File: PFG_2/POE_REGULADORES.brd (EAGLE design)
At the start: 119.6 x 95.9 mm, 185 parts, among them J1 1-406541-1, J10 OSTVN04A150, J2 AMPS_Connect, J3 Port Current, J4 OSTVN04A150, J5 TB001-500-02BE, J6 OSTVN02A150, J7 OSTVN02A150, J8 TB001-500-02BE, J9 TB001-500-02BE, Q1 FDN8601, Q2 FDN8601, Q3 FDN8601, Q4 FDN8601, Q5 CSD18533Q5A, Q6 CSD18533Q5A, T1 750313355, U1 7490220122, U10 12V, U11 FCX493TA, U12 TL431AIDBVR, U13 LM5165DRCR, U14 ENC28J60-I/SP, U2 TPS2373-3RGWT, U3 UCC2897APW, U4 12V, U5 FCX493TA, U6 TCMT1107, U7 MMBT3906, U8 FDMS86250, U9 IRFR9220PBF, Y1 Crystal_25Mhz

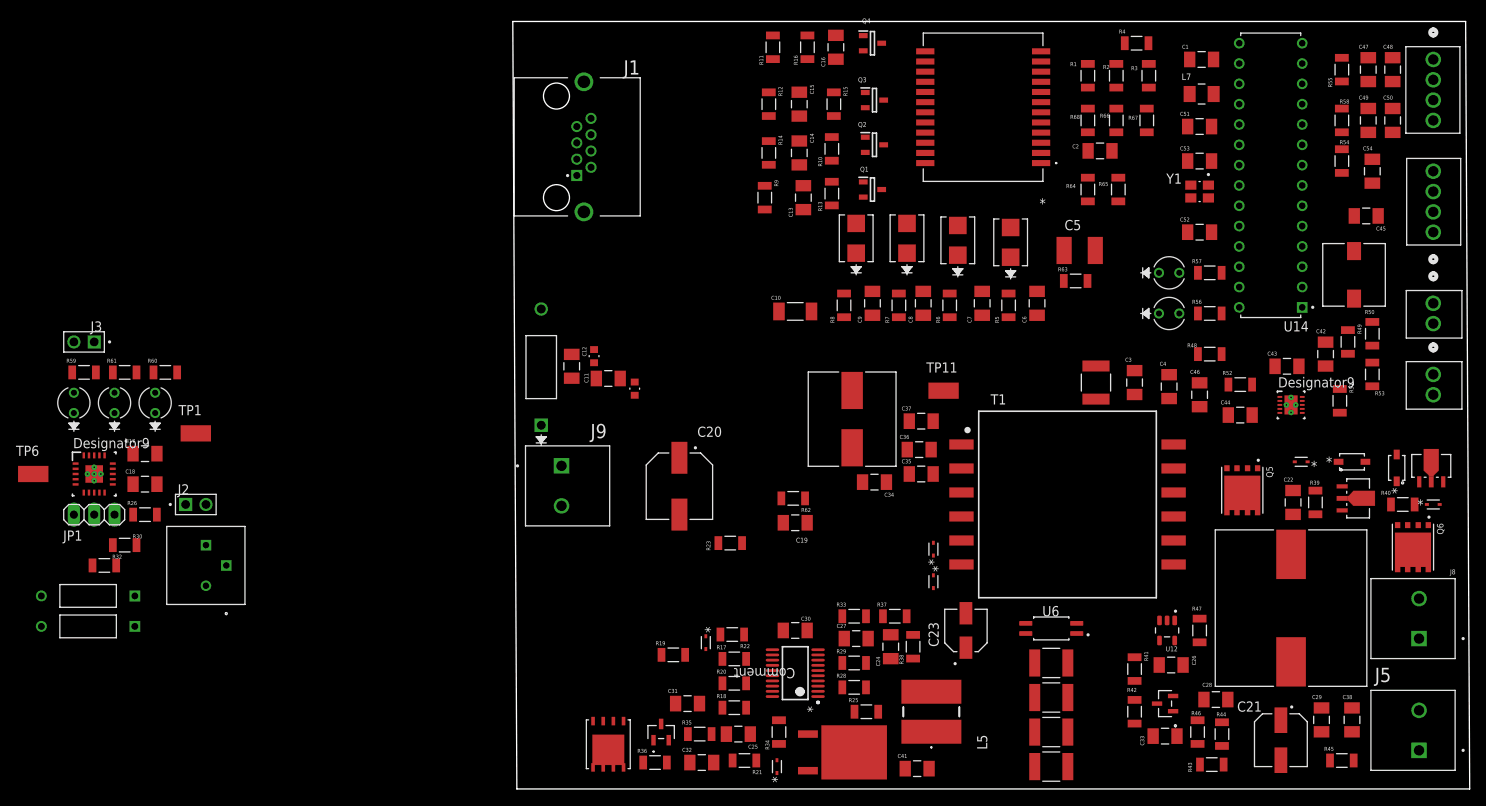
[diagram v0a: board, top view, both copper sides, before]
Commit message: Colocados componentes y planos RTN, GND, VDD, VSS, 3V3, 12V
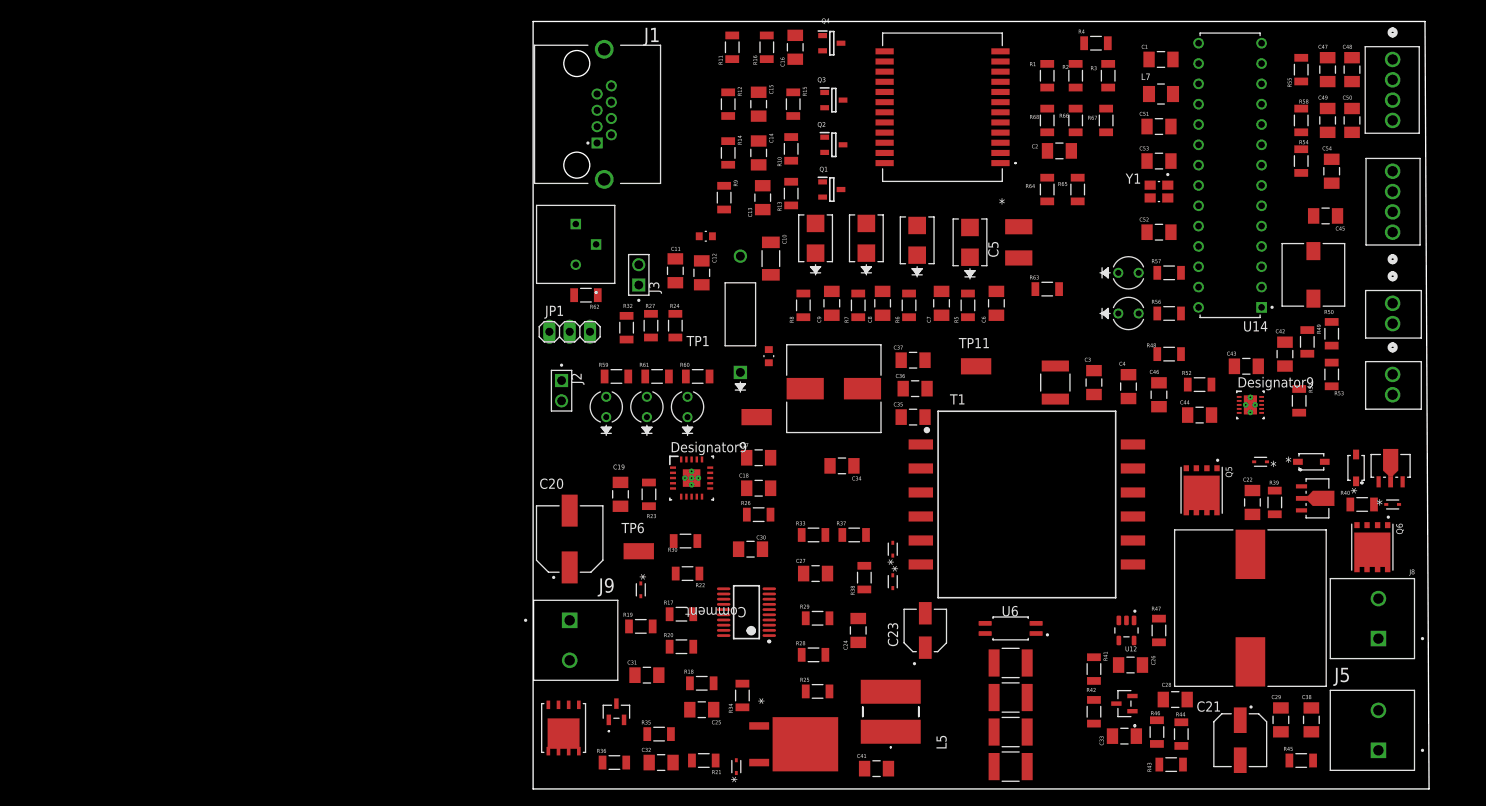
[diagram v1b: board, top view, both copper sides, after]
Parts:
- R24, R27: device R24:YAG_MF25_YAG -> RC1206FR-071ML:RESC3116X65N
- moved R24 77.3 mm to (19.8, 57.9), turned to 270 degrees
- moved C17 76.7 mm to (30.2, 41.4)
- moved C18 76.7 mm to (30.2, 37.6)
- moved R26 76.7 mm to (30.2, 34.3)
- moved TP6 76.3 mm to (15.2, 29.7)
- moved U2 74.7 mm to (21.8, 38.9)
- moved R27 72.8 mm to (16.8, 57.9), turned to 270 degrees
- moved R32 71.7 mm to (13.7, 57.7), turned to 270 degrees
- moved TP1 70.1 mm to (30.0, 46.5)
- moved R30 70.1 mm to (21.1, 31.0), turned to 0 degrees
- moved J3 69.8 mm to (15.2, 64.3), turned to 90 degrees
- moved LED1 66.5 mm to (16.3, 46.5)
- moved LED2 66.5 mm to (21.3, 46.5)
- moved LED3 66.5 mm to (11.2, 46.5)
- moved R59 66.5 mm to (12.4, 51.6)
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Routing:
- added copper zone on layer 15, net VSS
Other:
- board size 119.6 x 95.9 mm -> 112 x 95.9 mm

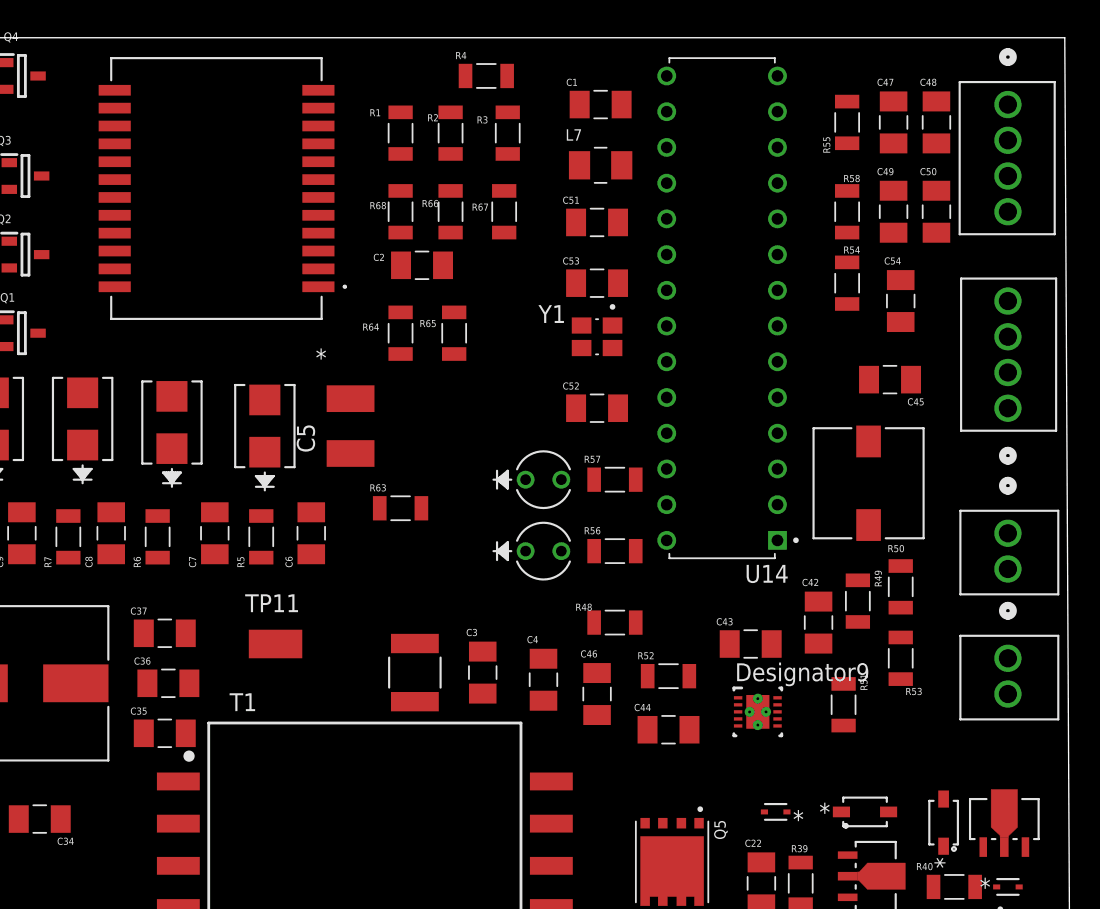
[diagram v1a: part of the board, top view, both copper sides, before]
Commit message: Colocadas pistas de zona 3V3
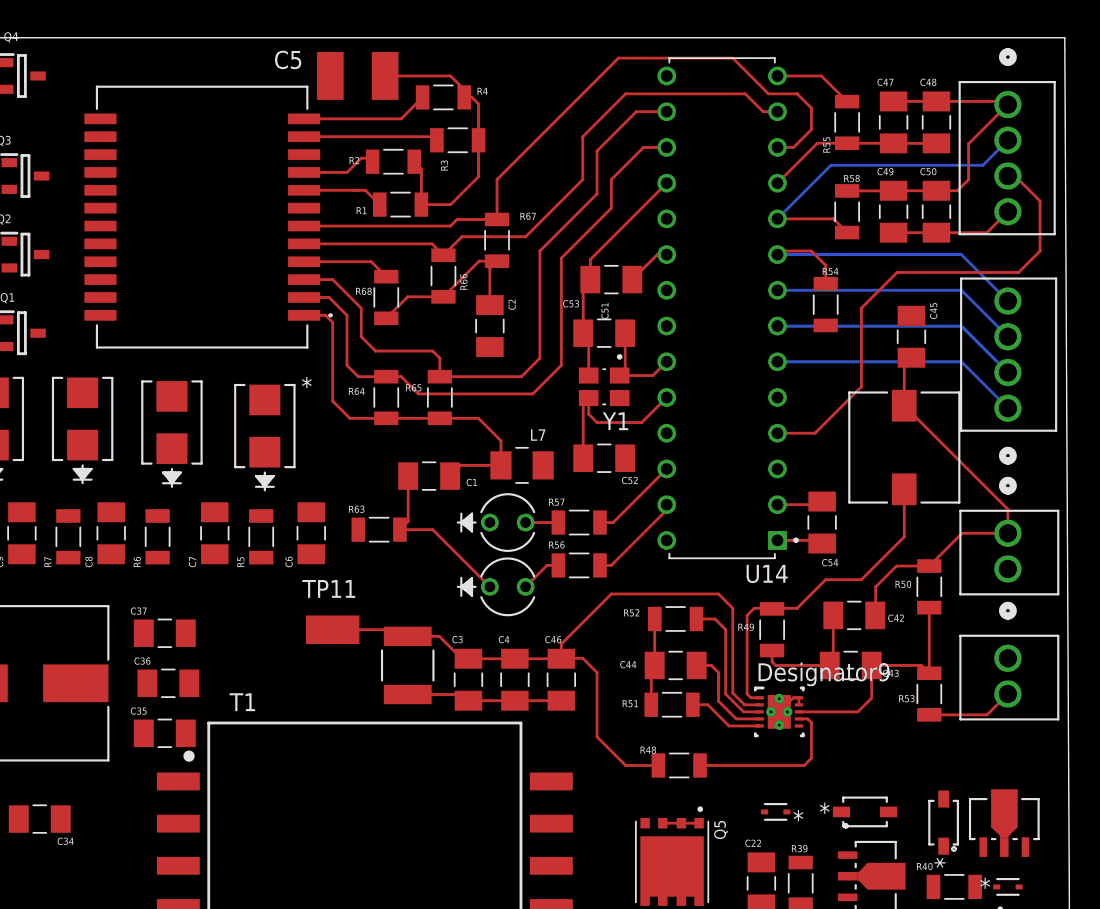
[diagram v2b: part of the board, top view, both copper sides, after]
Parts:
- moved C1 29.1 mm to (68.3, 64.8), turned to 180 degrees
- moved C5 24.9 mm to (63.2, 93.2), turned to 0 degrees
- moved L7 22.1 mm to (74.9, 65.5)
- moved C54 16.7 mm to (96.3, 61.5), turned to 270 degrees
- moved R51 12.2 mm to (85.6, 48.5), turned to 0 degrees
- moved R48 11.1 mm to (86.1, 44.2)
- moved C43 7.27 mm to (98.3, 51.3), turned to 180 degrees
- moved C2 6.48 mm to (72.6, 75.4), turned to 270 degrees
- moved R49 6.43 mm to (92.7, 53.8)
- moved R68 6.18 mm to (65.3, 77.5)
- moved R1 5.08 mm to (66.3, 84.1), turned to 0 degrees
- moved R65 4.68 mm to (69.1, 70.4)
- moved R64 4.68 mm to (65.3, 70.4)
- moved C44 4.60 mm to (85.9, 51.3)
- moved R66 4.60 mm to (69.3, 79.0)
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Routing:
- net GND: track 0.00 -> 81.3 mm
- net +3V3: track 0.00 -> 55.6 mm
- net VDD_P: track 0.00 -> 54.8 mm
- net RXD_N: track 0.00 -> 48.6 mm
- net TXD_N: track 0.00 -> 44.7 mm
- net TXD_P: track 0.00 -> 44.1 mm
- net RXD_P: track 0.00 -> 41.1 mm
- net N_INT: track 0.00 -> 33.9 mm
- net TXD_CT: track 0.00 -> 27.4 mm
- net RESET_ETH: track 0.00 -> 24.1 mm
- net N$70: track 0.00 -> 23.5 mm
- net CS: track 0.00 -> 23.0 mm
- net N$17: track 0.00 -> 21.1 mm
- net SPI_MOSI: track 0.00 -> 17.8 mm
- net SPI_SCLK: track 0.00 -> 17.8 mm
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
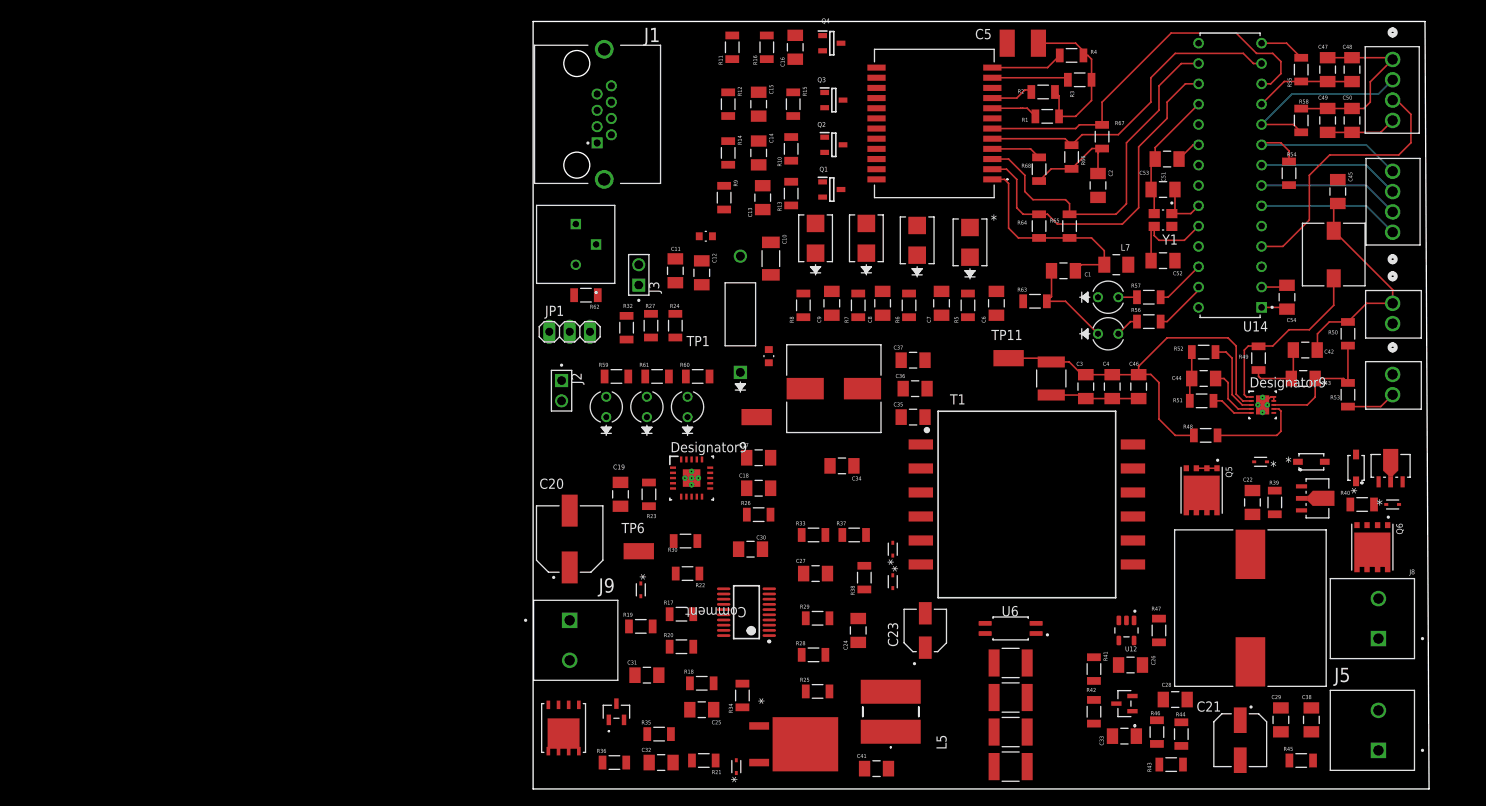
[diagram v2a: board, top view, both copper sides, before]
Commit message: Colocadas vias GND y RTN
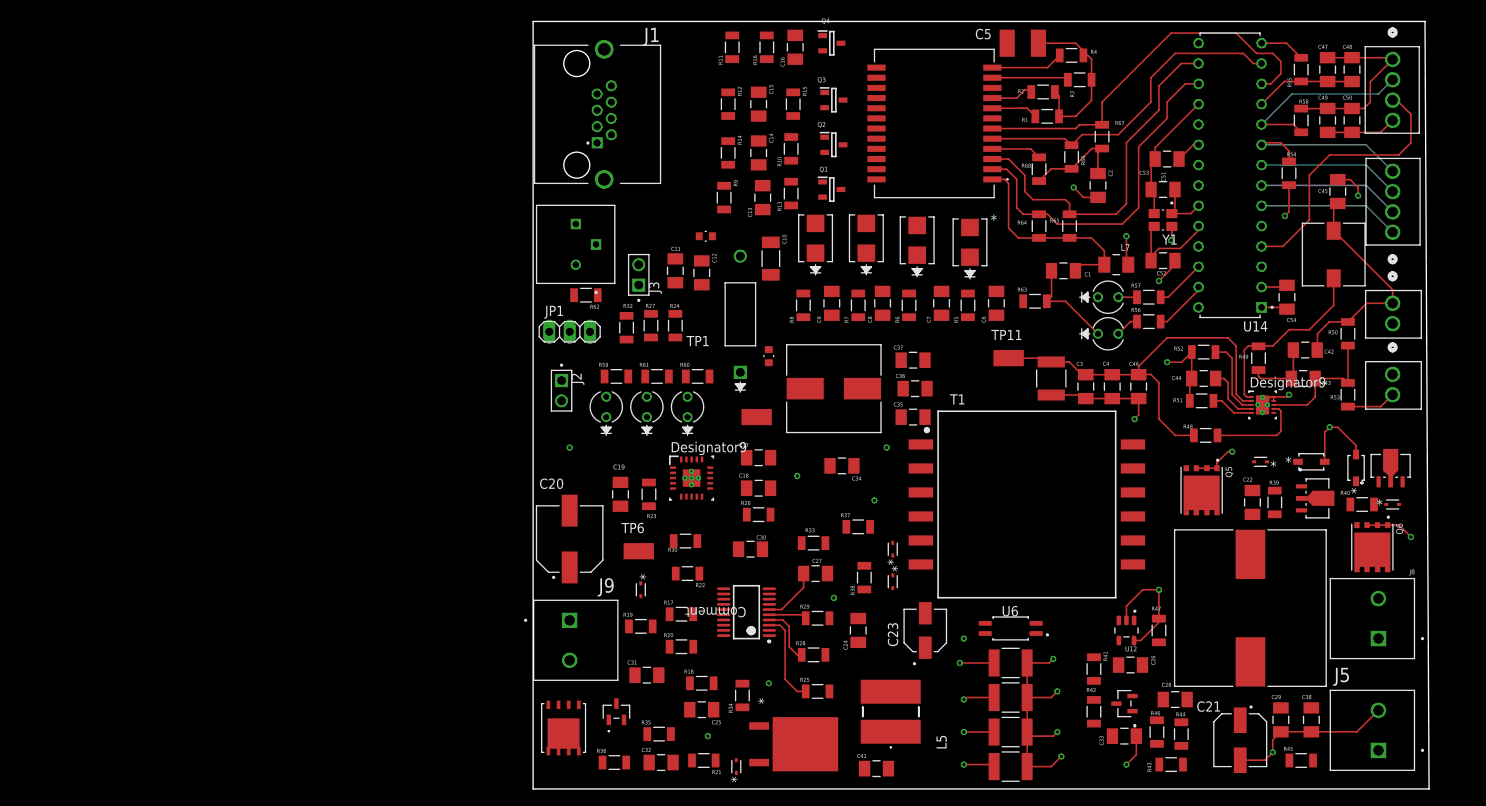
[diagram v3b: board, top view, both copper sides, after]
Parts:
- moved R37 1.14 mm to (42.7, 32.8)
- moved R33 1.02 mm to (37.1, 30.7), turned to 180 degrees
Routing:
- net GND: track 81.3 -> 190.6 mm, vias 0 -> 17
- net RTN: track 0.00 -> 15.8 mm, vias 0 -> 12
- net N$44: track 0.00 -> 11.6 mm
- net +3V3: track 55.6 -> 63.3 mm, vias 0 -> 2
- net N$45: track 0.00 -> 7.35 mm
- net N$48: track 0.00 -> 7.18 mm
- net N$46: track 0.00 -> 4.74 mm
- net OSC2: track 12.1 -> 12.8 mm

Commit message: Colocadas vias GND, RTN en cada componente, redistribución de componentes 12V
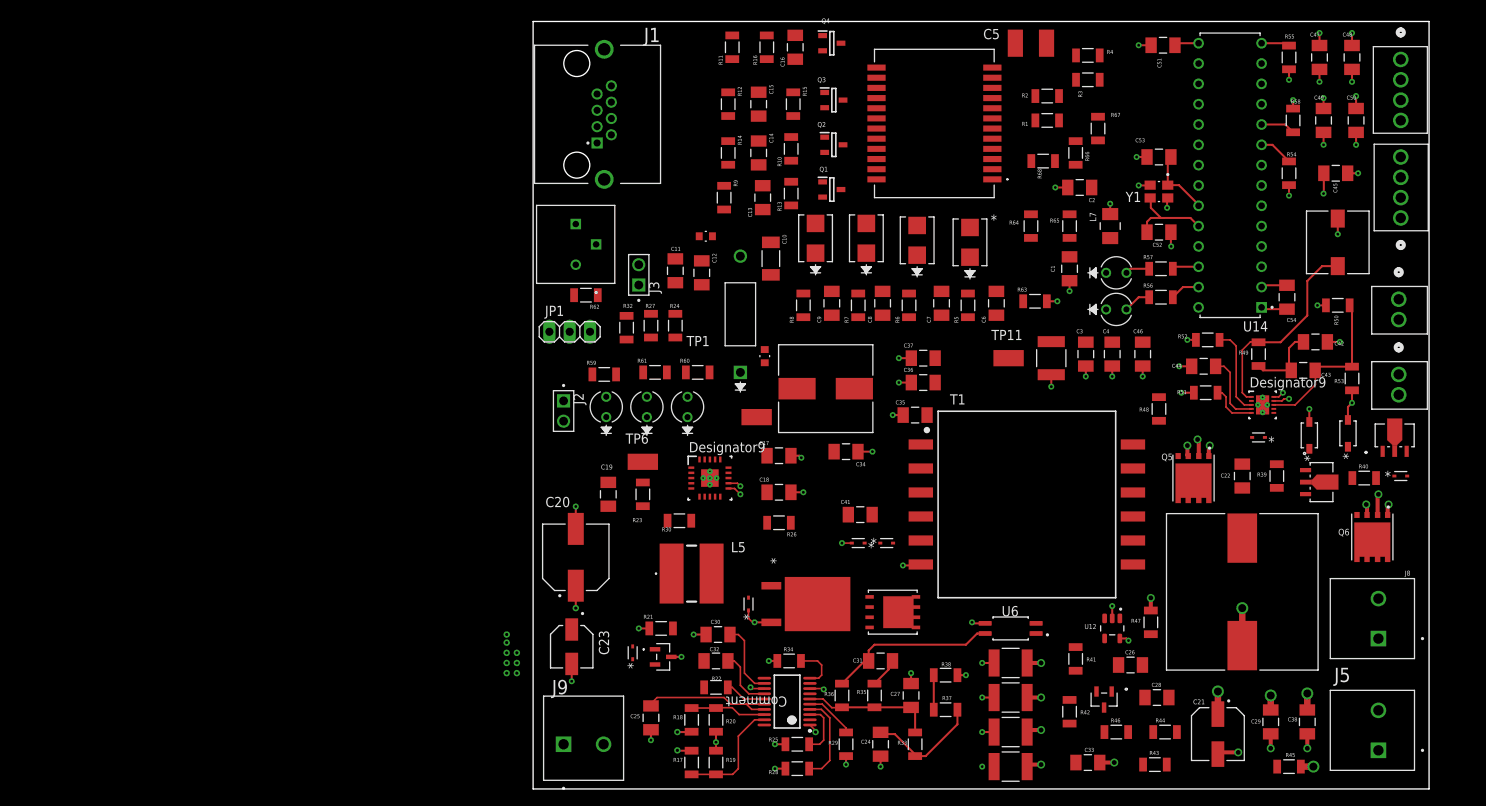
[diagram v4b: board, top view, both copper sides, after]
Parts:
- moved C23 44.2 mm to (6.86, 17.8), turned to 270 degrees
- moved U8 43.6 mm to (47.0, 22.1), turned to 0 degrees
- moved C41 31.8 mm to (42.9, 34.3)
- moved L5 30.3 mm to (21.8, 26.9), turned to 0 degrees
- moved R36 29.7 mm to (40.6, 11.7), turned to 270 degrees
- moved C31 29.3 mm to (45.5, 16.0)
- moved R33 28.2 mm to (49.8, 5.59), turned to 270 degrees
- moved R35 27.4 mm to (44.7, 11.7), turned to 270 degrees
- moved R37 25.3 mm to (53.6, 9.91), turned to 180 degrees
- moved D12 20.4 mm to (29.0, 23.1)
- moved R19 19.4 mm to (24.9, 3.30), turned to 270 degrees
- moved C27 19.4 mm to (49.3, 11.7), turned to 90 degrees
- moved R17 18.6 mm to (21.8, 3.30), turned to 270 degrees
- moved U9 17.6 mm to (37.6, 23.1)
- moved R21 17.4 mm to (18.0, 20.1), turned to 0 degrees
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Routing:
- net GND: track 190.6 -> 73.1 mm, vias 17 -> 42
- net VDD_P: track 54.8 -> 0.00 mm
- net RXD_N: track 48.6 -> 0.00 mm
- net +3V3: track 63.3 -> 18.6 mm, vias 2 -> 11
- net TXD_N: track 44.7 -> 0.00 mm
- net TXD_P: track 44.1 -> 0.00 mm
- net RXD_P: track 41.1 -> 0.00 mm
- net RTN: track 15.8 -> 51.1 mm, vias 12 -> 32
- net N_INT: track 33.9 -> 0.00 mm
- net TXD_CT: track 27.4 -> 0.00 mm
- net N$39: track 0.00 -> 21.3 mm
- net N$17: track 21.1 -> 0.00 mm
- net RESET_ETH: track 24.1 -> 4.34 mm
- net CS: track 23.0 -> 4.29 mm
- net SPI_MOSI: track 17.8 -> 0.00 mm
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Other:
- outline, holes or cut-outs redrawn

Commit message: Planos de masa y alimentación conectados a los componentes con vias
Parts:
- moved R48 25.9 mm to (55.1, 53.6)
- moved C10 17.1 mm to (15.2, 70.6)
- moved TP11 15.8 mm to (47.0, 47.5)
- moved R32 14.8 mm to (7.62, 44.2)
- moved R27 14.7 mm to (11.4, 44.2)
- moved R24 14.7 mm to (15.2, 43.9)
- moved C35 11.5 mm to (42.4, 55.6)
- moved C12 11.0 mm to (30.5, 56.4)
- moved TP6 10.9 mm to (5.08, 38.6)
- moved C11 10.3 mm to (30.0, 66.3)
- moved R26 9.96 mm to (24.9, 27.2), turned to 270 degrees
- moved C3 9.74 mm to (61.5, 55.6), turned to 180 degrees
- moved R62 9.11 mm to (4.06, 53.8)
- moved C18 8.62 mm to (30.7, 28.7)
- moved C46 8.30 mm to (70.6, 51.1), turned to 180 degrees
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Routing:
- net N$66: track 0.00 -> 59.1 mm, vias 0 -> 2
- net N$35: track 0.00 -> 58.9 mm
- net N$50: track 0.00 -> 50.1 mm, vias 0 -> 3
- net N$62: track 0.00 -> 39.5 mm, vias 0 -> 2
- net VC: track 17.6 -> 41.6 mm
- net VDD_P: track 0.00 -> 23.5 mm, vias 0 -> 11
- net VDD: track 7.57 -> 30.2 mm, vias 12 -> 11
- net N$38: track 0.00 -> 20.2 mm
- net N$39: track 21.3 -> 39.0 mm
- net N$47: track 14.4 -> 28.8 mm, vias 0 -> 2
- net N$65: track 0.00 -> 13.7 mm
- net N$34: track 0.00 -> 13.3 mm
- net N$37: track 0.00 -> 13.0 mm
- net N$63: track 0.00 -> 11.4 mm
- net VSS: track 0.00 -> 11.2 mm, vias 0 -> 7
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- added copper zone on layer 2, net BSVG
- added copper zone on layer 15, net VDD_P
- added copper zone on layer 15, net VSS1
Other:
- board size 112 x 95.9 mm -> 111.7 x 95.9 mm
